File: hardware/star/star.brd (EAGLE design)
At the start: 116.5 x 163.8 mm, 161 parts, among them IC1 MAX481CSA, IC2 LD117AS12TR, IC22 LD117AS12TR, IC3 74HCT08D, IC4 7404D, IC5 LM317MABDT, IC6 LM317MABDT, IC7 LM317MABDT, IC8 MAX481CSA, K1 T90-12VDC-TL-A, K2 T90-12VDC-TL-A, P1 B3B-PH-K, Q1 35A/25V/8.5mΩ, Q2 35A/25V/8.5mΩ, Q3 35A/25V/8.5mΩ, Q4 35A/25V/8.5mΩ, T1 T_PNP_MMBT5401_CHANGJ_SOT23-B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, T2 T_PNP_MMBT5401_CHANGJ_SOT23-B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, T3 T_PNP_MMBT5401_CHANGJ_SOT23-B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, T4 T_PNP_MMBT5401_CHANGJ_SOT23-B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, U1 TCLT1600, X1 MKDSN1,5/2-5,08, X3 MKDSN1,5/5-5,08

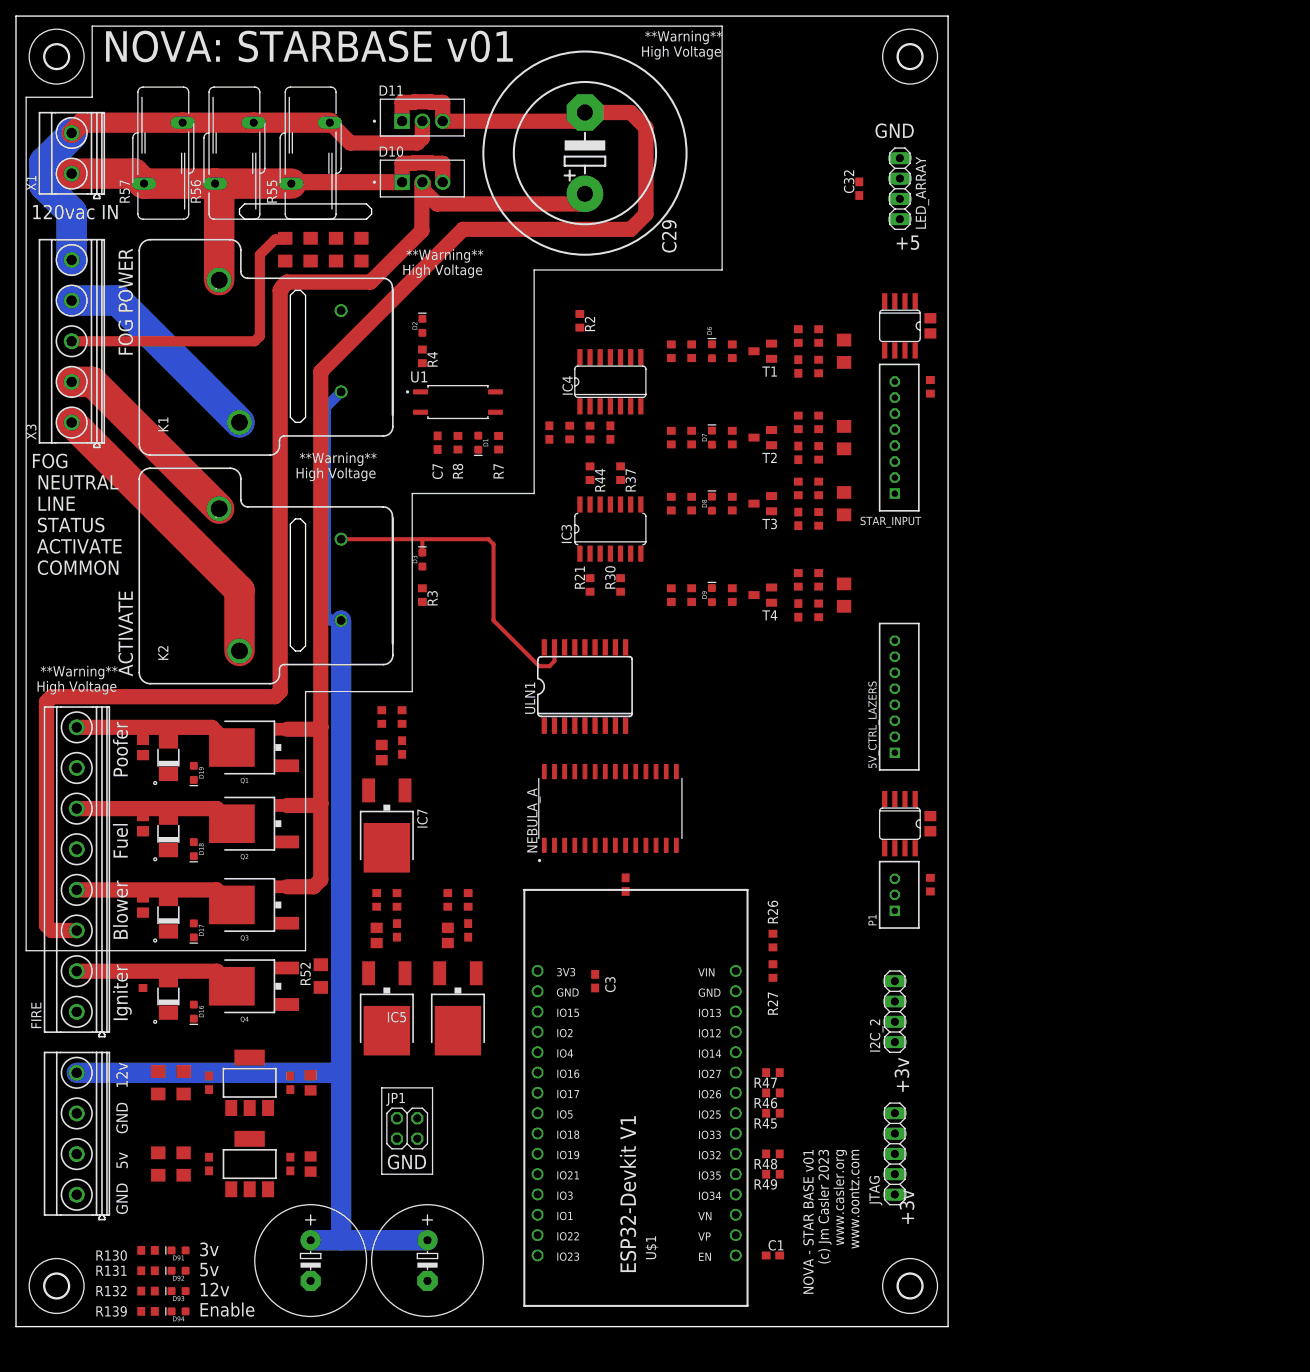
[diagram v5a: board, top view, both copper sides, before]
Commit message: critical traces routed
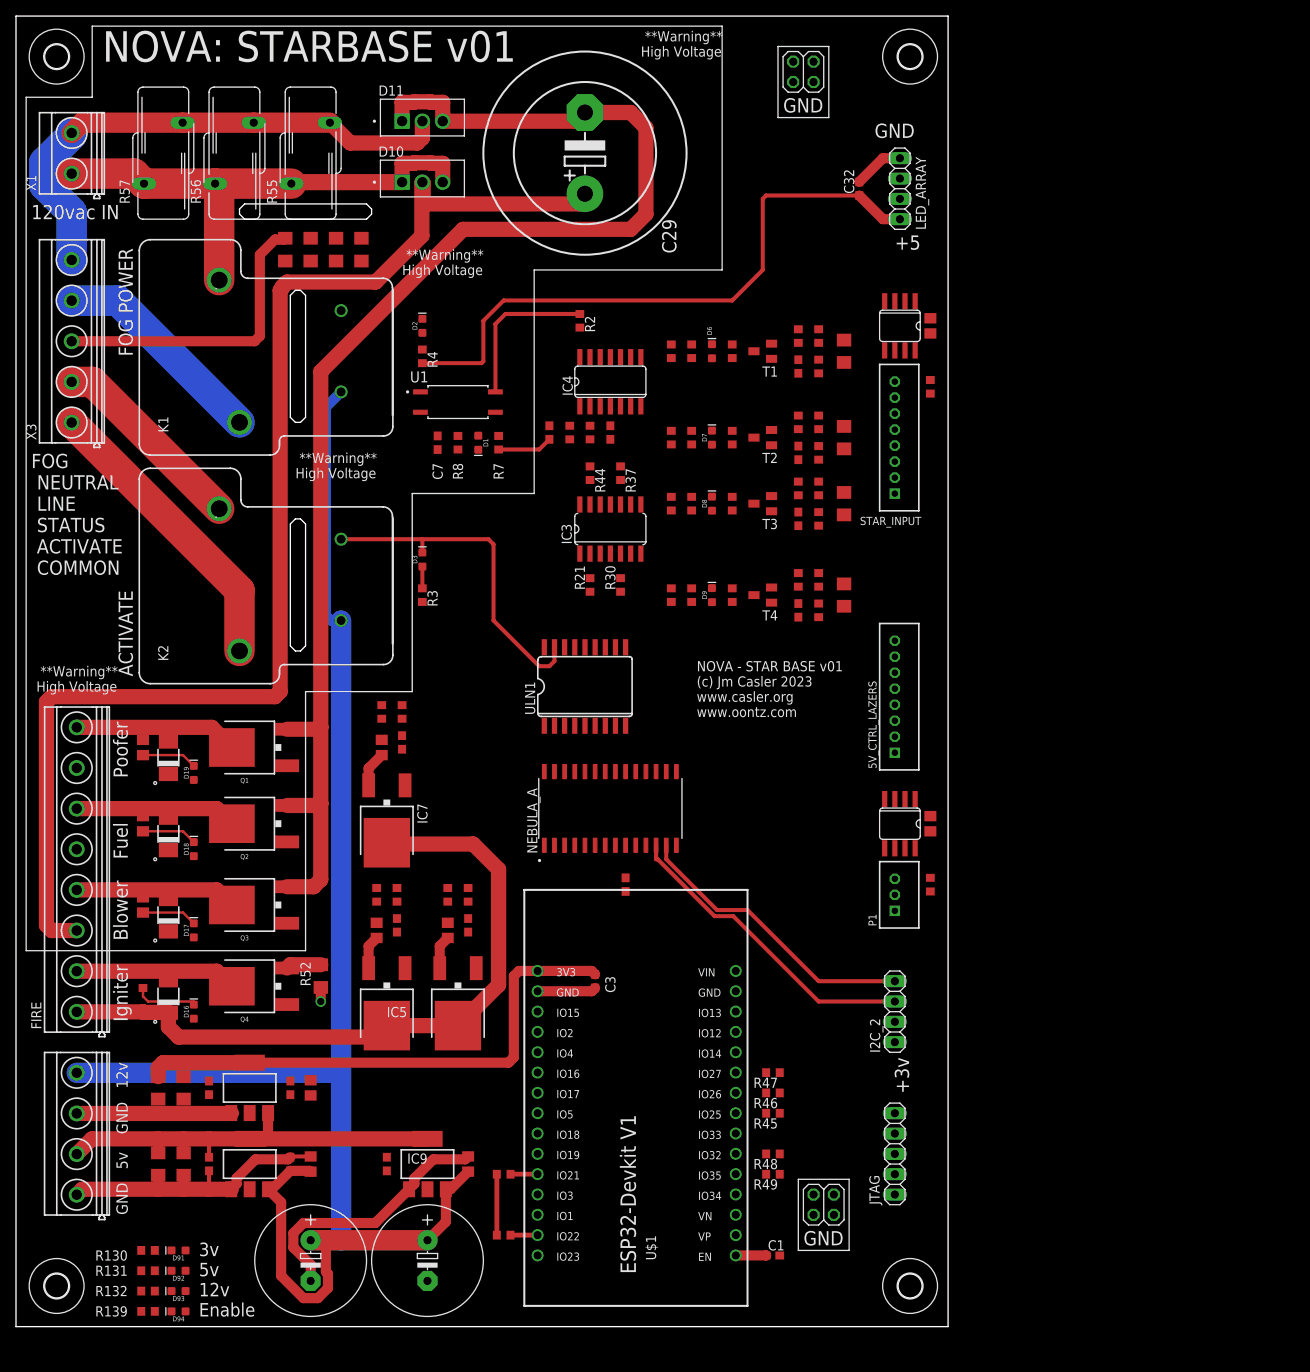
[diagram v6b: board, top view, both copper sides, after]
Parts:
- added C34: 1uf, rcl:C0805
- added C37: 10uf, rcl:C0603
- added IC9: LD117AS12TR, v-reg:SOT223
- added JP2: (no value), pinhead:2X02
- moved JP1 141.1 mm to (98.4, 156.8)
- moved R26 49.9 mm to (61.0, 11.4), turned to 180 degrees
- moved R27 42.2 mm to (61.0, 19.1), turned to 180 degrees
- moved C10 10.2 mm to (17.8, 20.3)
- moved C2 10.2 mm to (34.3, 20.3)
- moved C4 10.2 mm to (36.8, 20.3)
- moved C5 10.2 mm to (24.1, 20.3)
- moved C9 10.2 mm to (21.0, 20.3)
- moved IC2 10.2 mm to (29.2, 20.3)
- moved C11 9.52 mm to (21.0, 29.8)
- moved C12 9.52 mm to (17.8, 29.8)
- moved C35 9.52 mm to (34.3, 29.8)
- moved C36 9.52 mm to (24.1, 29.8)
- moved C6 9.52 mm to (36.8, 29.8)
- moved IC22 9.52 mm to (29.2, 29.8)
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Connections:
- net +12V: now also C34.1, IC9.3
- net +5V: now also C37.1, IC9.4
- net GND: now also C34.2, C37.2, IC9.1, JP2.1, JP2.2, JP2.3, JP2.4
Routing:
- net +5V: track 0.00 -> 131.6 mm
- net GND: track 0.00 -> 112.2 mm, vias 0 -> 1
- net +6V: track 0.00 -> 86.9 mm
- net +3V3: track 0.00 -> 74.5 mm
- net +12V: track 155.4 -> 225.3 mm
- net 22/SCL: track 0.00 -> 42.3 mm
- net 21/SDA: track 0.00 -> 40.0 mm
- net N$2: track 0.00 -> 19.6 mm
- net N$54: track 0.00 -> 8.06 mm
- net N$55: track 0.00 -> 6.91 mm
- net N$57: track 0.00 -> 6.91 mm
- net N$56: track 0.00 -> 6.91 mm
- net GND3: track 0.00 -> 4.39 mm
- net N$1: track 0.00 -> 3.80 mm
- net N$4: track 0.00 -> 2.72 mm
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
